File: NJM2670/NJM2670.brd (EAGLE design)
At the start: 11 parts, among them J1 AVR_SPI_PRG_62X3_LOCK

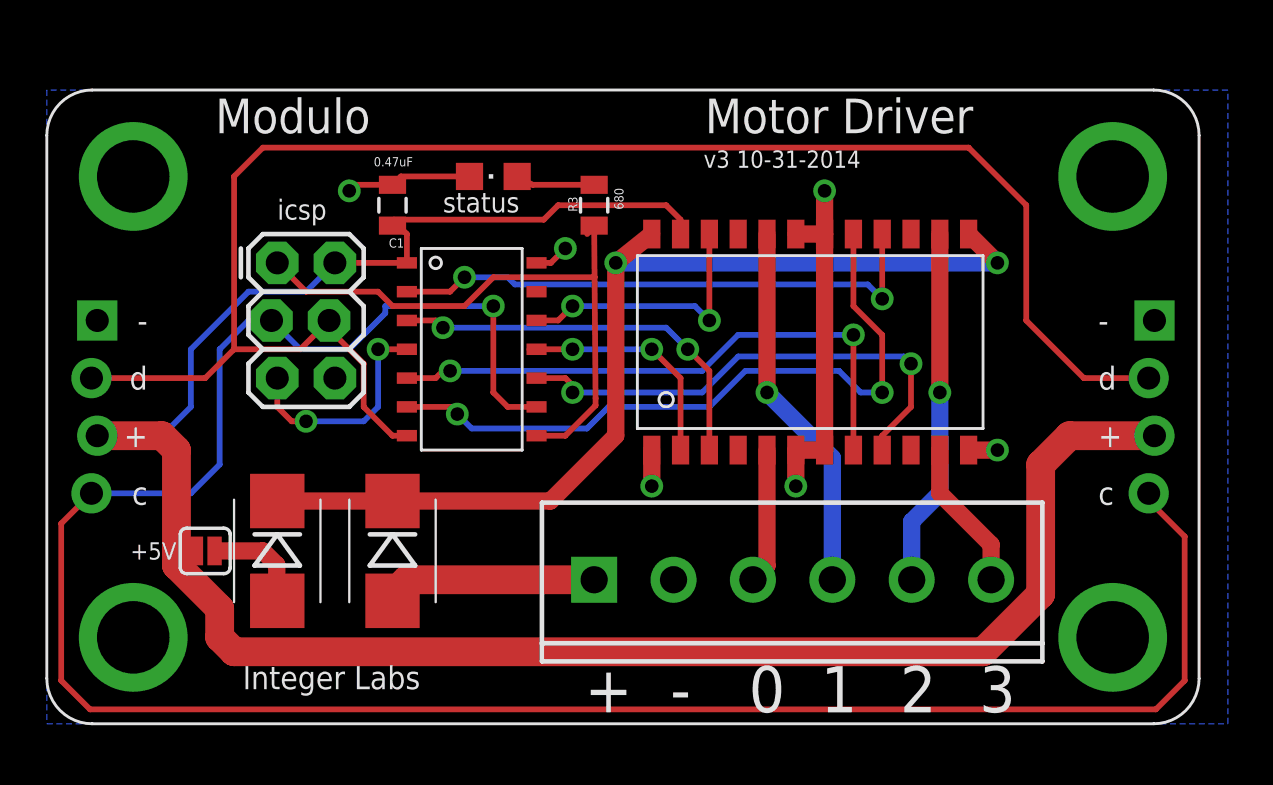
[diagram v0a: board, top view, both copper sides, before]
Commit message: Reverted to old version of motor driver board
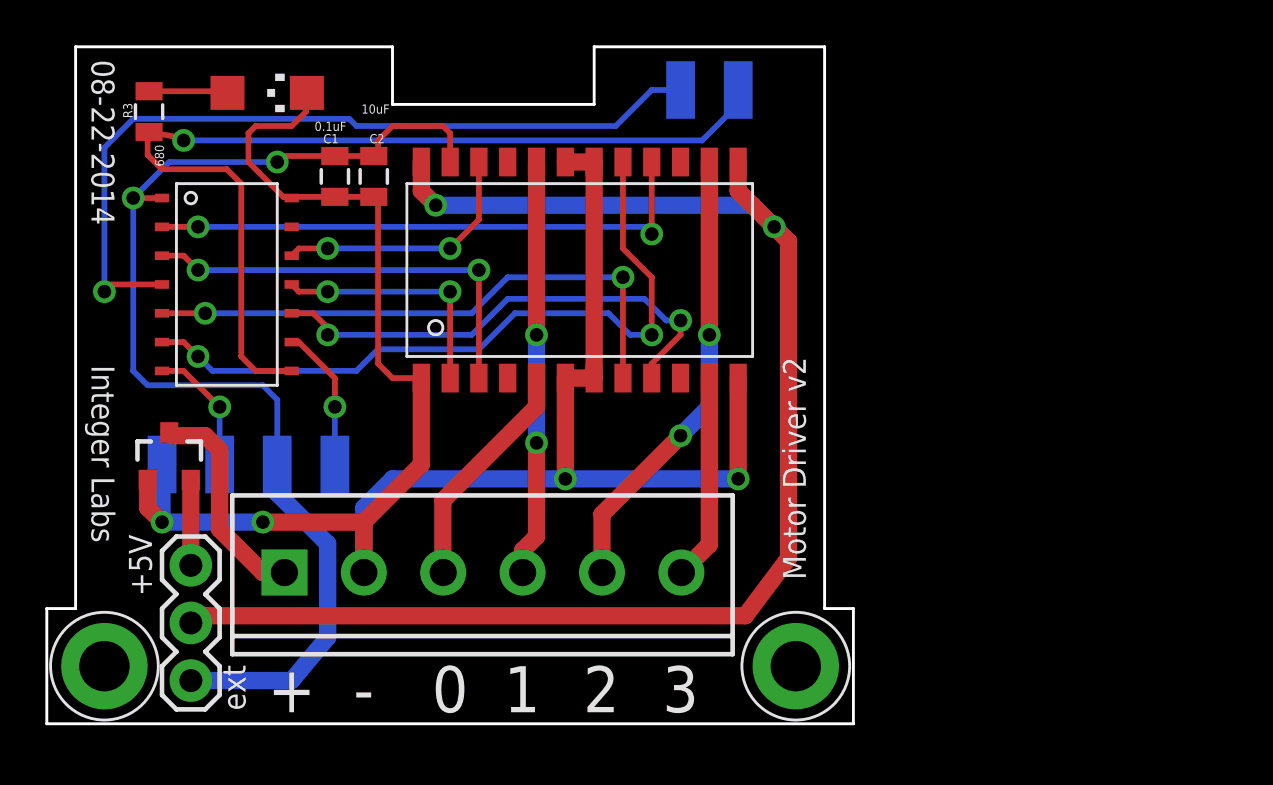
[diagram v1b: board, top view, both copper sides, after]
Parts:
- removed D1, D2: (no value), SparkFun-DiscreteSemi:SMB-DIODE
- removed J1: AVR_SPI_PRG_62X3_LOCK, SparkFun-Connectors:2X3_LOCK
- removed LED1: (no value), adafruit:CHIPLED_0805
- removed SJ1: SOLDERJUMPERNC, SparkFun-Passives:SJ_2S
- removed U$1: FOOTPRINT3-4U, IntegerLabs:FOOTPRINT3-4U
- added C2: 10uF, SparkFun-Capacitors:0805
- added JP3: (no value), SparkFun-Connectors:1X03
- added LED: blue, led:CHIPLED_1206
- added Q1: MOSFET-PCHANNELIRLML2244, SparkFun-DiscreteSemi:SOT23-3
- added U$4: FOOTPRINTFOOTPRINT-2, IntegerLabs:FOOTPRINT2
- C1: value 0.47uF -> 0.1uF
- moved R3 20.1 mm to (4.51, 27.0)
- moved JP4 13.7 mm to (10.5, 6.67)
- moved U$3 11.2 mm to (8.26, 23.2)
- moved U$6 10.6 mm to (22.9, 19.7)
- moved C1 2.84 mm to (12.7, 24.1), turned to 90 degrees
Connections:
- net GND: now also C2.1, LED.C, Q1.1, U$4.GND; no longer J1.6, LED1.C, U$1.GNDL, U$1.GNDR
- net MISO/LED: now also U$4.MISO; no longer J1.1
- net N$1: now also JP3.3, Q1.2; no longer D1.A, SJ1.2
- net N$5: now also LED.A; no longer LED1.A
- net RESET: now also U$4.RESET; no longer J1.5
- net SCL/SCK: now also U$4.SCL; no longer J1.3, U$1.SCLL, U$1.SCLR
- net SDA/MOSI: now also U$4.SDA; no longer J1.4, U$1.SDAL, U$1.SDAR
- net VCC: now also C2.2, JP3.1, U$4.VCC; no longer J1.2, SJ1.1, U$1.VCCL, U$1.VCCR
- net VIN: now also Q1.3; no longer D2.A
- net VS: now also JP3.2; no longer D1.C, D2.C
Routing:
- net SCL/SCK: track 99.6 -> 6.37 mm
- net SDA/MOSI: track 74.1 -> 5.74 mm, vias 0 -> 1
- net GND: track 25.5 -> 84.9 mm, vias 6 -> 4
- net VCC: track 96.9 -> 51.1 mm, vias 0 -> 2
- net RESET: track 10.1 -> 35.7 mm, vias 2 -> 1
- net VS: track 44.4 -> 63.6 mm
- net MISO/LED: track 26.9 -> 43.6 mm, vias 0 -> 1
- net N$11: track 5.97 -> 10.3 mm
- net N$13: track 15.8 -> 20.1 mm, vias 1 -> 2
- net N$14: track 6.65 -> 9.08 mm
- net N$12: track 16.4 -> 18.4 mm, vias 1 -> 2
- net INB2: track 30.3 -> 31.7 mm
- net ENABLEA: track 17.7 -> 19.0 mm
- net N$1: track 4.60 -> 3.76 mm
- net TSD: track 24.5 -> 25.1 mm
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- removed copper zone on layer 16, net GND
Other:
- board outline added: 35.6 x 29.8 mm
- board text added: "08-22-2014"
- board text added: "Motor Driver v2"
- board text added: "ext"
- board text removed: "Modulo"
- board text removed: "Motor Driver"
- board text removed: "c"
- board text removed: "d"
- board text removed: "icsp"
- board text removed: "status"
- board text removed: "v3 10-31-2014"

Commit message: New linear/inline layout of motor driver board
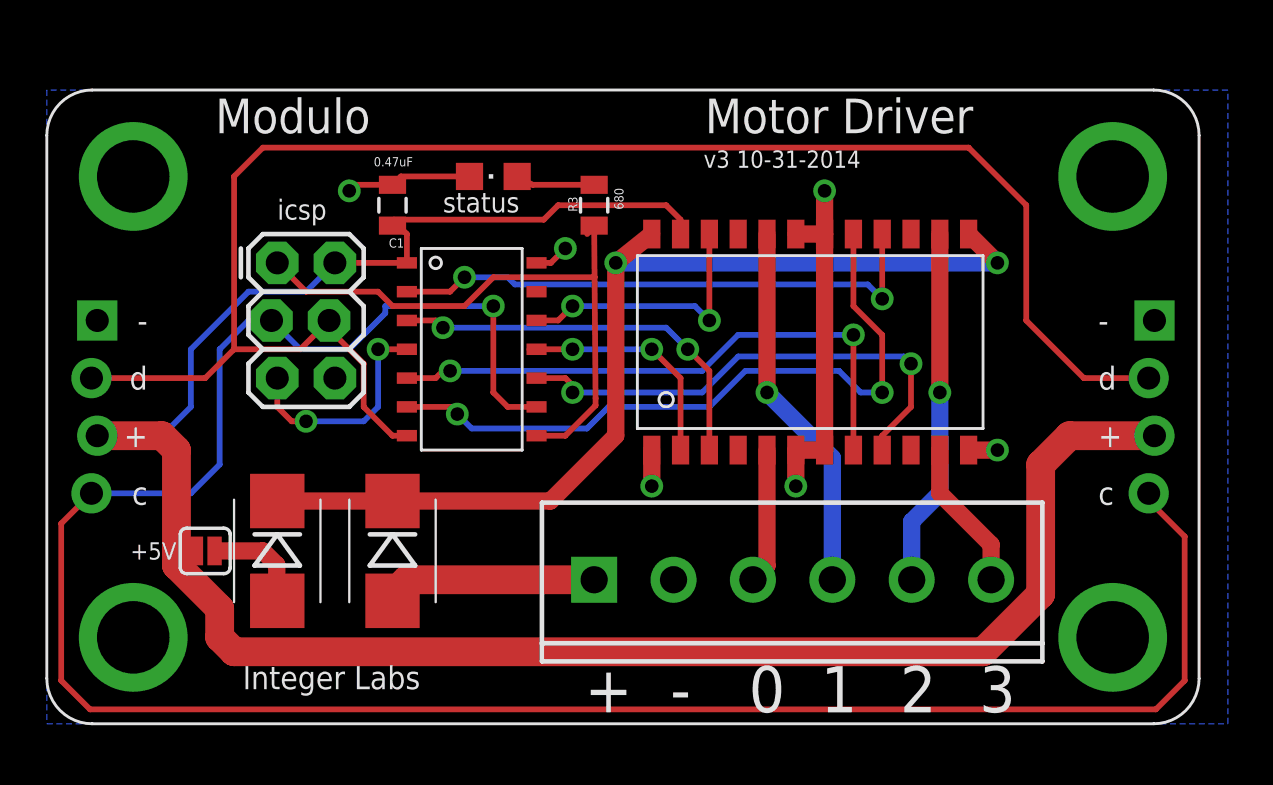
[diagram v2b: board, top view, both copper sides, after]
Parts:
- removed C2: 10uF, SparkFun-Capacitors:0805
- removed JP3: (no value), SparkFun-Connectors:1X03
- removed LED: blue, led:CHIPLED_1206
- removed Q1: MOSFET-PCHANNELIRLML2244, SparkFun-DiscreteSemi:SOT23-3
- removed U$4: FOOTPRINTFOOTPRINT-2, IntegerLabs:FOOTPRINT2
- added D1, D2: (no value), SparkFun-DiscreteSemi:SMB-DIODE
- added J1: AVR_SPI_PRG_62X3_LOCK, SparkFun-Connectors:2X3_LOCK
- added LED1: (no value), adafruit:CHIPLED_0805
- added SJ1: SOLDERJUMPERNC, SparkFun-Passives:SJ_2S
- added U$1: FOOTPRINT3-4U, IntegerLabs:FOOTPRINT3-4U
- C1: value 0.1uF -> 0.47uF
- moved R3 20.1 mm to (24.1, 22.9)
- moved JP4 13.7 mm to (24.1, 6.35)
- moved U$3 11.2 mm to (19.1, 20.3)
- moved U$6 10.6 mm to (33.0, 16.5)
- moved C1 2.84 mm to (15.2, 22.9), turned to 270 degrees
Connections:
- net GND: now also J1.6, LED1.C, U$1.GNDL, U$1.GNDR; no longer C2.1, LED.C, Q1.1, U$4.GND
- net MISO/LED: now also J1.1; no longer U$4.MISO
- net N$1: now also D1.A, SJ1.2; no longer JP3.3, Q1.2
- net N$5: now also LED1.A; no longer LED.A
- net RESET: now also J1.5; no longer U$4.RESET
- net SCL/SCK: now also J1.3, U$1.SCLL, U$1.SCLR; no longer U$4.SCL
- net SDA/MOSI: now also J1.4, U$1.SDAL, U$1.SDAR; no longer U$4.SDA
- net VCC: now also J1.2, SJ1.1, U$1.VCCL, U$1.VCCR; no longer C2.2, JP3.1, U$4.VCC
- net VIN: now also D2.A; no longer Q1.3
- net VS: now also D1.C, D2.C; no longer JP3.2
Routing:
- net SCL/SCK: track 6.37 -> 99.6 mm
- net SDA/MOSI: track 5.74 -> 74.1 mm, vias 1 -> 0
- net GND: track 84.9 -> 25.5 mm, vias 4 -> 6
- net VCC: track 51.1 -> 96.9 mm, vias 2 -> 0
- net RESET: track 35.7 -> 10.1 mm, vias 1 -> 2
- net VS: track 63.6 -> 44.4 mm
- net MISO/LED: track 43.6 -> 26.9 mm, vias 1 -> 0
- net N$11: track 10.3 -> 5.97 mm
- net N$13: track 20.1 -> 15.8 mm, vias 2 -> 1
- net N$14: track 9.08 -> 6.65 mm
- net N$12: track 18.4 -> 16.4 mm, vias 2 -> 1
- net INB2: track 31.7 -> 30.3 mm
- net ENABLEA: track 19.0 -> 17.7 mm
- net N$1: track 3.76 -> 4.60 mm
- net TSD: track 25.1 -> 24.5 mm
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- added copper zone on layer 16, net GND
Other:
- board outline removed
- board text added: "Modulo"
- board text added: "Motor Driver"
- board text added: "c"
- board text added: "d"
- board text added: "icsp"
- board text added: "status"
- board text added: "v3 10-31-2014"
- board text removed: "08-22-2014"
- board text removed: "Motor Driver v2"
- board text removed: "ext"
